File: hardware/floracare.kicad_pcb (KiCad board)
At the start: 2 copper layers, 100 x 100 mm, 26 parts, among them J2 Conn_01x04_Socket, J4 Conn_01x04_Socket, J5 Conn_01x14_Socket, J6 Conn_01x05_Socket, SW1 SW_Push, SW2 SW_Push, U1 AMS1117-3.3, U2 ESP32-S3-WROOM-1

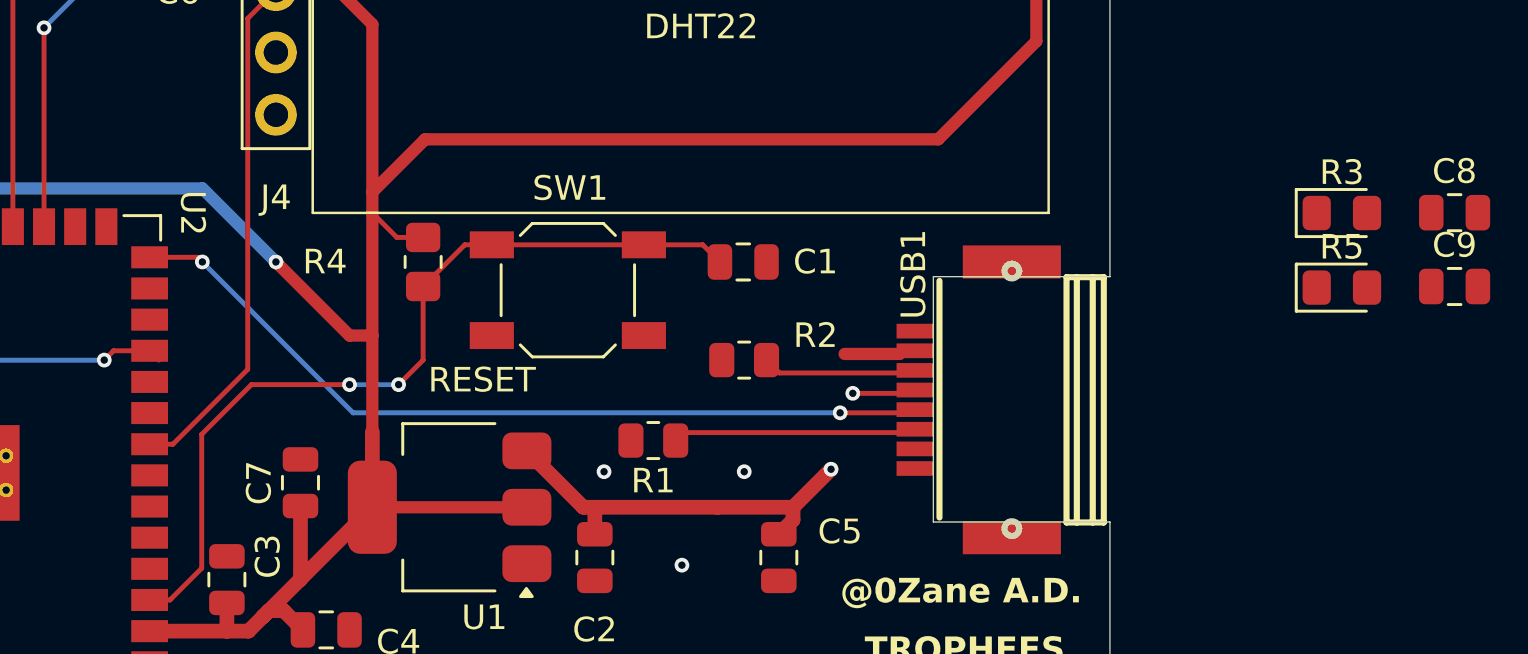
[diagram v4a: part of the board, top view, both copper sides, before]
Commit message: Rounting UCBC 8 pin
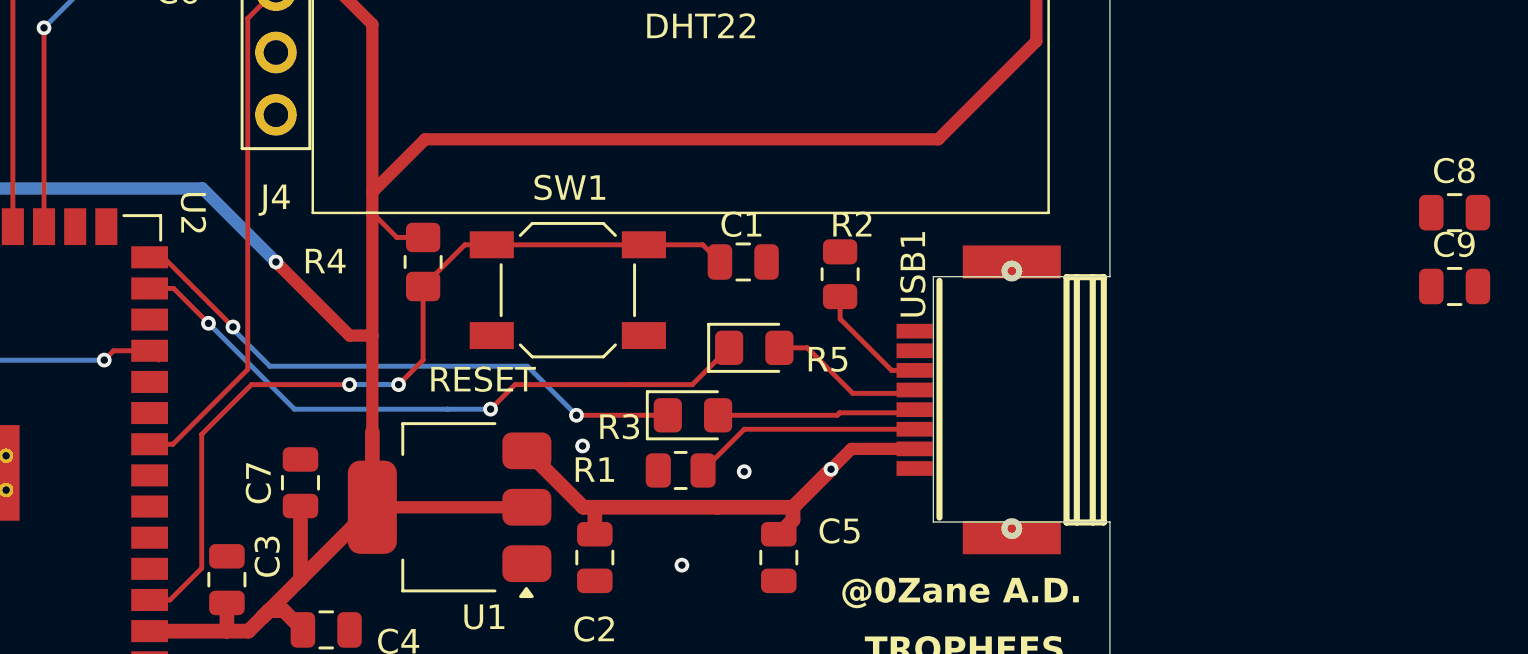
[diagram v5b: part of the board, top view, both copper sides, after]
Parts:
- moved R3 27.7 mm to (223.4, 106.1)
- moved R5 24.1 mm to (225.9, 103.3)
- moved R2 5.25 mm to (229.4, 100.3), turned to 90 degrees
- moved R1 1.65 mm to (222.9, 108.3)
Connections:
- USB1 pad B9: +5V -> unconnected-(USB1-VBUS-PadB9)
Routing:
- net Net-(U2-USB_D-): track 0.00 -> 26.9 mm, vias 0 -> 2
- net Net-(U2-USB_D+): track 34.3 -> 23.9 mm
- net DATA+: track 0.00 -> 8.49 mm
- net DATA-: track 2.96 -> 6.72 mm, vias 1 -> 0
- net +5V: track 18.8 -> 20.3 mm
- net Net-(USB1-CC2): track 6.28 -> 4.83 mm
- net Net-(USB1-CC1): track 10.3 -> 9.33 mm
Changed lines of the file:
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@@
 	(net 54 "Net-(U2-USB_D+)")
 	(net 55 "Net-(U2-USB_D-)")
+	(net 56 "unconnected-(USB1-VBUS-PadB9)")
 	(footprint "Resistor_SMD:R_0805_2012Metric_Pad1.20x1.40mm_HandSolder"
 		(layer "F.Cu")
@@
 	(footprint "Resistor_SMD:R_0805_2012Metric"
 		(layer "F.Cu")
-		(at 221.8035 107.13 180)
+		(at 222.92 108.35 180)
 		(descr "Resistor SMD 0805 (2012 Metric), square (rectangular) end terminal, IPC-7351 nominal, (Body size source: IPC-SM-782 page 72, https://www.pcb-3d.com/wordpress/wp-content/uploads/ipc-sm-782a_amendment_1_and_2.pdf), generated with kicad-footprint-generator")
 		(tags "resistor")
 		(property "Reference" "R1"
-			(at 0 -1.65 0)
+			(at 3.5 0 0)
 			(layer "F.SilkS")
 			(effects
@@
 	(footprint "Resistor_SMD:R_0805_2012Metric"
 		(layer "F.Cu")
-		(at 225.5075 103.85 180)
+		(at 229.42 100.35 90)
 		(descr "Resistor SMD 0805 (2012 Metric), square (rectangular) end terminal, IPC-7351 nominal, (Body size source: IPC-SM-782 page 72, https://www.pcb-3d.com/wordpress/wp-content/uploads/ipc-sm-782a_amendment_1_and_2.pdf), generated with kicad-footprint-generator")
 		(tags "resistor")
 		(property "Reference" "R2"
-			(at -2.9125 1 0)
+			(at 2 0.5 180)
 			(layer "F.SilkS")
 			(effects
@@
 		)
 		(property "Value" "5.1K"
-			(at 3.0875 -1 0)
+			(at 3.0875 -1 90)
 			(layer "F.Fab")
 			(effects
@@
 		)
 		(property "Datasheet" "~"
-			(at 0 0 0)
+			(at 0 0 90)
 			(layer "F.Fab")
 			(hide yes)
@@
 		)
 		(property "Description" "Resistor"
-			(at 0 0 0)
+			(at 0 0 90)
 			(layer "F.Fab")
 			(hide yes)
@@
 		(attr smd)
 		(fp_line
-			(start -0.227064 0.735)
-			(end 0.227064 0.735)
+			(start -0.227064 -0.735)
+			(end 0.227064 -0.735)
 			(stroke
 				(width 0.12)
@@
 		)
 		(fp_line
-			(start -0.227064 -0.735)
-			(end 0.227064 -0.735)
+			(start -0.227064 0.735)
+			(end 0.227064 0.735)
 			(stroke
 				(width 0.12)
@@
 		)
 		(fp_text user "${REFERENCE}"
-			(at 0 0 0)
+			(at 0 0 90)
 			(layer "F.Fab")
 			(effects
@@
 		)
 		(pad "1" smd roundrect
-			(at -0.9125 0 180)
+			(at -0.9125 0 90)
 			(size 1.025 1.4)
 			(layers "F.Cu" "F.Mask" "F.Paste")
@@
 		)
 		(pad "2" smd roundrect
-			(at 0.9125 0 180)
+			(at 0.9125 0 90)
 			(size 1.025 1.4)
 			(layers "F.Cu" "F.Mask" "F.Paste")
@@
 	(footprint "LED_SMD:LED_0805_2012Metric_Pad1.15x1.40mm_HandSolder"
 		(layer "F.Cu")
-		(at 249.875 100.895)
+		(at 225.92 103.35)
 		(descr "LED SMD 0805 (2012 Metric), square (rectangular) end terminal, IPC-7351 nominal, (Body size source: https://docs.google.com/spreadsheets/d/1BsfQQcO9C6DZCsRaXUlFlo91Tg2WpOkGARC1WS5S8t0/edit?usp=sharing), generated with kicad-footprint-generator")
 		(tags "LED handsolder")
 		(property "Reference" "R5"
-			(at 0 -1.65 0)
+			(at 3 0.5 0)
 			(layer "F.SilkS")
 			(effects
@@
 		)
 		(property "Value" "22"
-			(at 0 1.65 0)
+			(at -2.955 4.455 0)
 			(layer "F.Fab")
 			(effects
@@
 			(size 0.6 1.5)
 			(layers "F.Cu" "F.Mask" "F.Paste")
-			(net 3 "+5V")
+			(net 56 "unconnected-(USB1-VBUS-PadB9)")
 			(pinfunction "VBUS")
-			(pintype "unspecified")
+			(pintype "unspecified+no_connect")
 		)
 		(pad "B12" smd rect
@@
 		(tags "capacitor")
 		(property "Reference" "C1"
-			(at 2.95 0 0)
+			(at -0.05 -1.5 0)
 			(layer "F.SilkS")
 			(effects
@@
 	(footprint "LED_SMD:LED_0805_2012Metric_Pad1.15x1.40mm_HandSolder"
 		(layer "F.Cu")
-		(at 249.875 97.855)
+		(at 223.42 106.1)
 		(descr "LED SMD 0805 (2012 Metric), square (rectangular) end terminal, IPC-7351 nominal, (Body size source: https://docs.google.com/spreadsheets/d/1BsfQQcO9C6DZCsRaXUlFlo91Tg2WpOkGARC1WS5S8t0/edit?usp=sharing), generated with kicad-footprint-generator")
 		(tags "LED handsolder")
 		(property "Reference" "R3"
-			(at 0 -1.65 0)
+			(at -3 0.5 0)
 			(layer "F.SilkS")
 			(effects
@@
 		)
 		(property "Value" "22"
-			(at 0 1.65 0)
+			(at 1.5 -1.25 0)
 			(layer "F.Fab")
 			(effects
@@
 		)
 	)
+	(segment
+		(start 231.86 106)
+		(end 229.4 106)
+		(width 0.2)
+		(layer "F.Cu")
+		(net 1)
+	)
+	(segment
+		(start 229.3 106.1)
+		(end 224.445 106.1)
+		(width 0.2)
+		(layer "F.Cu")
+		(net 1)
+	)
+	(segment
+		(start 231.866 106.006)
+		(end 231.86 106)
+		(width 0.2)
+		(layer "F.Cu")
+		(net 1)
+	)
+	(segment
+		(start 229.4 106)
+		(end 229.3 106.1)
+		(width 0.2)
+		(layer "F.Cu")
+		(net 1)
+	)
+	(segment
+		(start 232.8945 106.006)
+		(end 231.866 106.006)
+		(width 0.2)
+		(layer "F.Cu")
+		(net 1)
+	)
 	(via
 		(at 161.375 76.65)
@@
 	)
 	(via
-		(at 219.795 108.4)
+		(at 218.92 107.35)
 		(size 0.6)
 		(drill 0.3)
@@
 	)
 	(segment
-		(start 229.6 103.6)
-		(end 231.86 103.6)
-		(width 0.5)
-		(layer "F.Cu")
-		(net 3)
-	)
-	(segment
 		(start 219.42 109.85)
 		(end 219.42 110.95)
@@
 	)
 	(segment
+		(start 229.88 107.47)
+		(end 229.05 108.3)
+		(width 0.5)
+		(layer "F.Cu")
+		(net 3)
+	)
+	(segment
 		(start 218.95 109.85)
 		(end 219.42 109.85)
@@
 		(net 3)
 	)
+	(segment
+		(start 232.47 107.47)
+		(end 229.88 107.47)
+		(width 0.5)
+		(layer "F.Cu")
+		(net 3)
+	)
 	(via
 		(at 229.05 108.3)
@@
 	)
 	(segment
+		(start 229.936 105.206)
+		(end 228.08 103.35)
+		(width 0.2)
+		(layer "F.Cu")
+		(net 4)
+	)
+	(segment
 		(start 232.8945 105.206)
 		(end 229.936 105.206)
@@
 		(net 4)
 	)
-	(via
-		(at 229.936 105.206)
-		(size 0.6)
-		(drill 0.3)
-		(layers "F.Cu" "B.Cu")
+	(segment
+		(start 228.08 103.35)
+		(end 226.945 103.35)
+		(width 0.2)
+		(layer "F.Cu")
 		(net 4)
 	)
@@
 	)
 	(segment
-		(start 232.8945 106.806)
-		(end 223.04 106.806)
+		(start 225.5125 106.67)
+		(end 232.47 106.67)
 		(width 0.2)
 		(layer "F.Cu")
@@
 	)
 	(segment
-		(start 223.04 106.806)
-		(end 222.716 107.13)
+		(start 223.8325 108.35)
+		(end 225.5125 106.67)
 		(width 0.2)
 		(layer "F.Cu")
@@
 	)
 	(segment
-		(start 226.944 104.374)
-		(end 226.42 103.85)
+		(start 231.52 104.27)
+		(end 229.42 102.17)
+		(width 0.2)
+		(layer "F.Cu")
+		(net 51)
+	)
+	(segment
+		(start 232.47 104.27)
+		(end 231.52 104.27)
 		(width 0.2)
 		(layer "F.Cu")
@@
 	)
 	(segment
-		(start 232.482 104.374)
-		(end 226.944 104.374)
+		(start 229.42 102.17)
+		(end 229.42 101.2625)
 		(width 0.2)
 		(layer "F.Cu")
@@
 	)
 	(segment
-		(start 201.27 99.66)
-		(end 203.23 99.66)
+		(start 201.828527 99.66)
+		(end 201.27 99.66)
 		(width 0.2)
 		(layer "F.Cu")
@@
 	)
 	(segment
-		(start 231.86 106)
-		(end 229.4 106)
+		(start 222.395 106.1)
+		(end 218.67 106.1)
 		(width 0.2)
 		(layer "F.Cu")
@@
 	)
 	(segment
-		(start 203.23 99.66)
-		(end 203.42 99.85)
+		(start 204.669 102.500473)
+		(end 201.828527 99.66)
 		(width 0.2)
 		(layer "F.Cu")
 		(net 54)
 	)
+	(via
+		(at 218.67 106.1)
+		(size 0.6)
+		(drill 0.3)
+		(layers "F.Cu" "B.Cu")
+		(net 54)
+	)
+	(via
+		(at 204.669 102.500473)
+		(size 0.6)
+		(drill 0.3)
+		(layers "F.Cu" "B.Cu")
+		(net 54)
+	)
 	(segment
-		(start 231.866 106.006)
-		(end 231.86 106)
+		(start 218.67 106.1)
+		(end 216.67 104.1)
 		(width 0.2)
-		(layer "F.Cu")
+		(layer "B.Cu")
 		(net 54)
 	)
 	(segment
-		(start 232.8945 106.006)
-		(end 231.866 106.006)
+		(start 204.669 102.599)
+		(end 204.669 102.500473)
 		(width 0.2)
-		(layer "F.Cu")
+		(layer "B.Cu")
+		(net 54)
+	)
+	(segment
+		(start 206.17 104.1)
+		(end 204.669 102.599)
+		(width 0.2)
+		(layer "B.Cu")
+		(net 54)
+	)
+	(segment
+		(start 216.67 104.1)
+		(end 206.17 104.1)
+		(width 0.2)
+		(layer "B.Cu")
 		(net 54)
 	)
+	(segment
+		(start 224.895 103.35)
+		(end 223.395 104.85)
+		(width 0.2)
+		(layer "F.Cu")
+		(net 55)
+	)
+	(segment
+		(start 202.25 100.93)
+		(end 203.67 102.35)
+		(width 0.2)
+		(layer "F.Cu")
+		(net 55)
+	)
+	(segment
+		(start 201.27 100.93)
+		(end 202.25 100.93)
+		(width 0.2)
+		(layer "F.Cu")
+		(net 55)
+	)
+	(segment
+		(start 220.92 104.85)
+		(end 221.17 104.85)
+		(width 0.2)
+		(layer "F.Cu")
+		(net 55)
+	)
+	(segment
+		(start 223.395 104.85)
+		(end 220.92 104.85)
+		(width 0.2)
+		(layer "F.Cu")
+		(net 55)
+	)
+	(segment
+		(start 220.92 104.85)
+		(end 216.17 104.85)
+		(width 0.2)
+		(layer "F.Cu")
+		(net 55)
+	)
+	(segment
+		(start 216.17 104.85)
+		(end 215.17 105.85)
+		(width 0.2)
+		(layer "F.Cu")
+		(net 55)
+	)
 	(via
-		(at 203.42 99.85)
+		(at 203.67 102.35)
 		(size 0.6)
 		(drill 0.3)
 		(layers "F.Cu" "B.Cu")
-		(net 54)
+		(net 55)
 	)
 	(via
-		(at 229.42 106)
+		(at 215.17 105.85)
 		(size 0.6)
 		(drill 0.3)
 		(layers "F.Cu" "B.Cu")
-		(net 54)
+		(net 55)
 	)
 	(segment
-		(start 209.57 106)
-		(end 229.4 106)
+		(start 203.67 102.35)
+		(end 207.17 105.85)
 		(width 0.2)
 		(layer "B.Cu")
-		(net 54)
+		(net 55)
 	)
 	(segment
-		(start 203.42 99.85)
-		(end 209.57 106)
+		(start 207.17 105.85)
+		(end 213.42 105.85)
 		(width 0.2)
 		(layer "B.Cu")
-		(net 54)
+		(net 55)
+	)
+	(segment
+		(start 213.42 105.85)
+		(end 215.17 105.85)
+		(width 0.2)
+		(layer "B.Cu")
+		(net 55)
 	)
 	(embedded_fonts no)

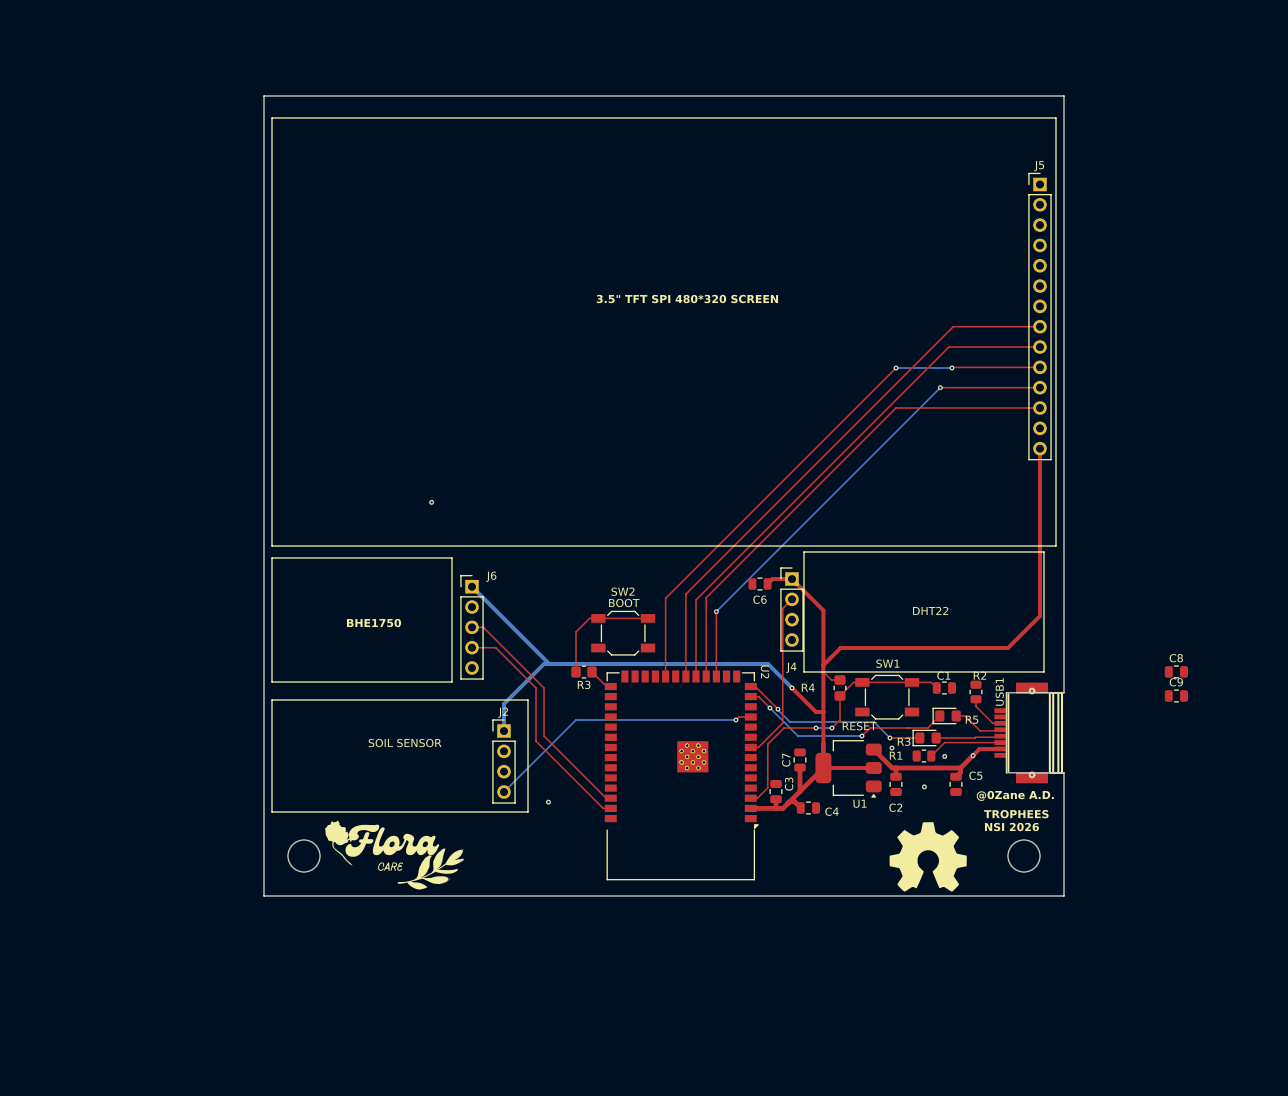
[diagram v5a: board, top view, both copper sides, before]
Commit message: Finishing PCB , [USBC NOT STABLE WITH DRC]
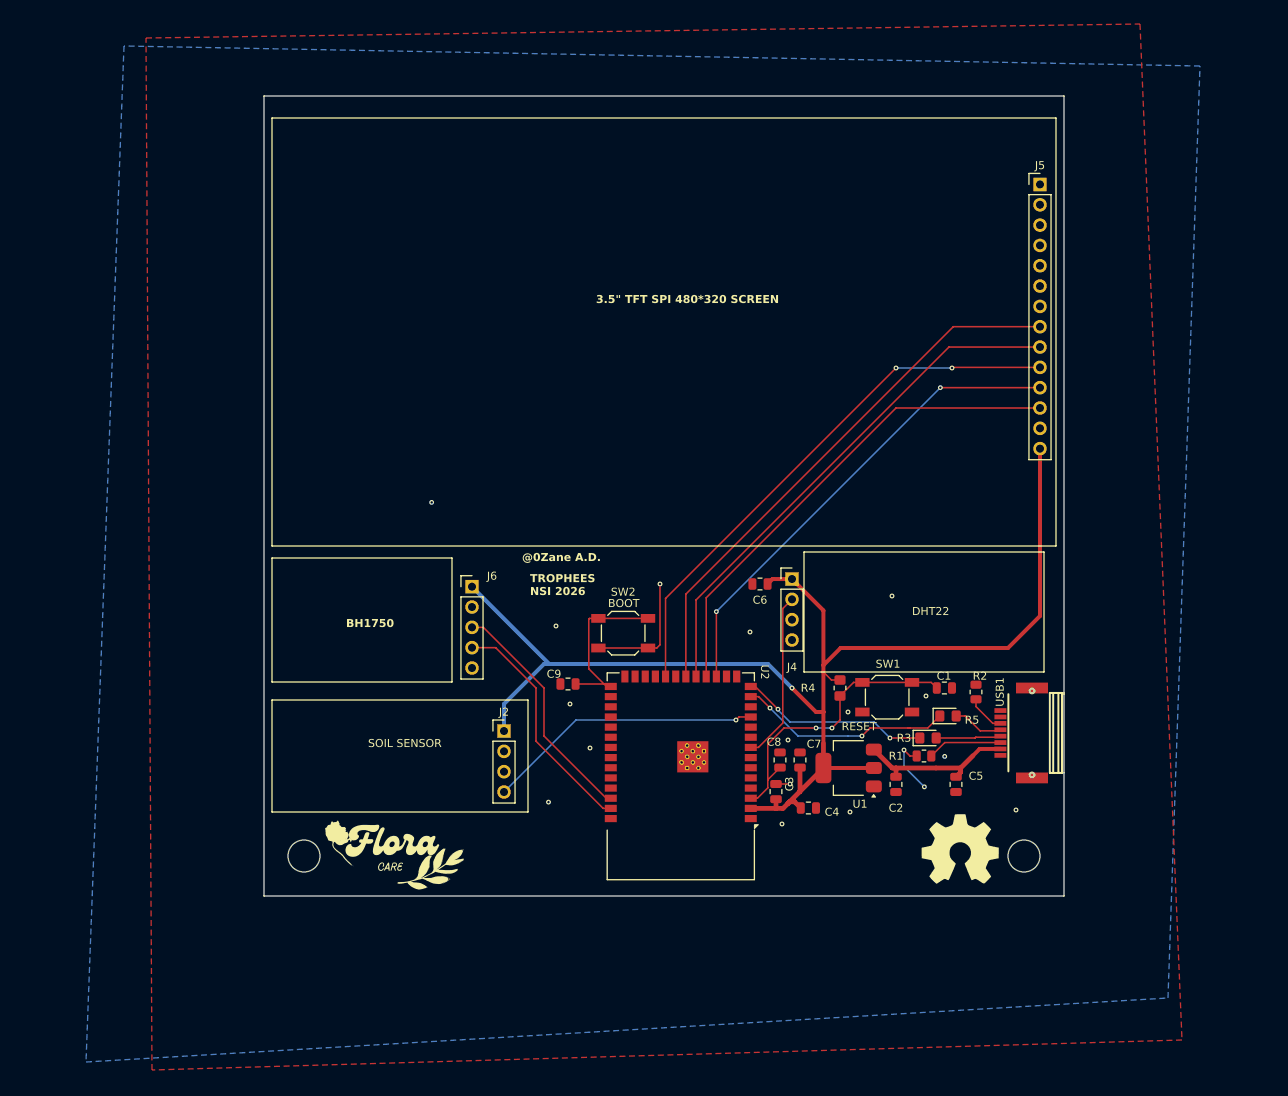
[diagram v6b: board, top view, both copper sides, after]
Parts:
- removed the R3 at (180.4, 97.8)
- moved C9 76.1 mm to (178.4, 99.3)
- moved C8 50.8 mm to (204.9, 108.8), turned to 90 degrees
- moved G*** 4.12 mm to (227.4, 119.8)
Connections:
- C9 pad 2: unconnected-(C9-Pad2) -> BOOT
- SW2 pad 2: +3V3 -> GND
- USB1 pad A9: +5V -> unconnected-(USB1-VBUS-PadA9)
- USB1 pad B9: unconnected-(USB1-VBUS-PadB9) -> +5V
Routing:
- net GND: track 0.00 -> 24.8 mm, vias 5 -> 18
- net BOOT: track 3.10 -> 21.8 mm
- net Net-(R3-Pad2): track 14.7 -> 0.00 mm
- net RESET: track 34.5 -> 36.7 mm
- net +5V: vias 1 -> 0
- added copper zone on B.Cu, net GND
- added copper zone on F.Cu, net GND
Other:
- outline, holes or cut-outs redrawn
- board text added: "BH1750"
- board text removed: "BHE1750"
